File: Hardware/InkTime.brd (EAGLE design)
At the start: 46 x 35 mm, 105 parts, among them IC1 BQ25180YBGR, IC2 DRV2605YZFR, IC3 BMA423, IC9 RT6160AWSC, J1 503480-2400, J2 TC2030-IDC, J4 KH-TYPE-C-16P, Q1 20V/4.2A/52mΩ/1.4W, Q3 SI1308EDL-T1-GE3, U1 NRF52840_QF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

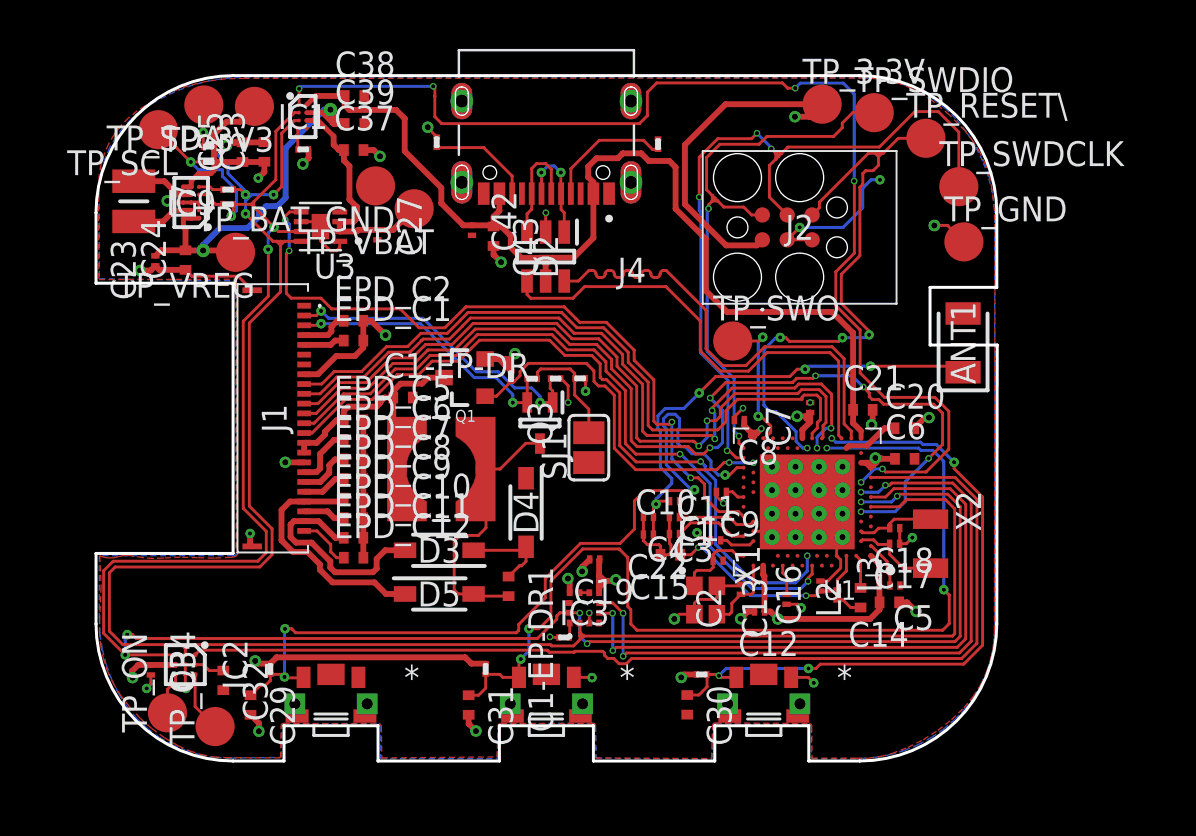
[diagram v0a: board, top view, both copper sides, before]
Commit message: Fixed #1. Added README.md, and updated the schematic and PCB design as stated in the issue.
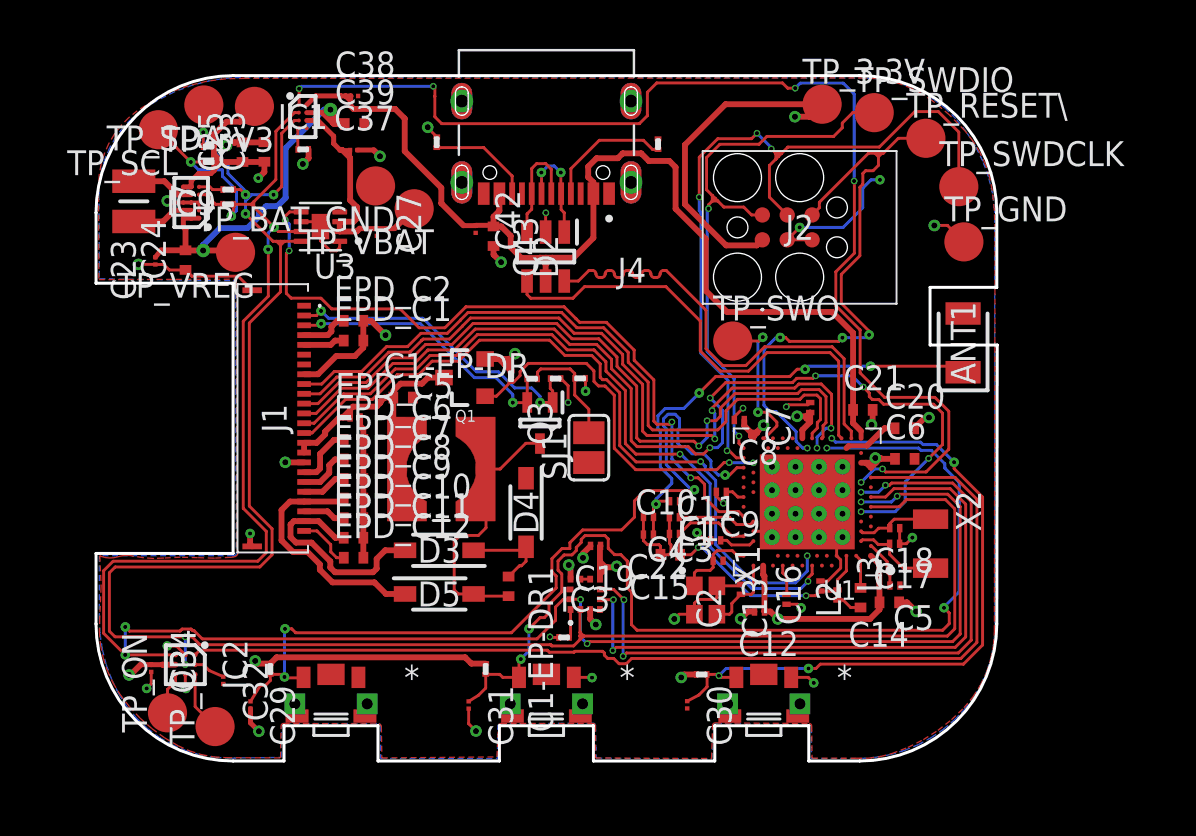
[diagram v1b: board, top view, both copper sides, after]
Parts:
- C23, C27, C34, C42: device InkTime_v5:NORDIC_NRF_3_RESC0201_L -> InkTime_v5:GRM011R60J152KE01L_2_CAPC0201X13N
- C29, C30, C31, C32, C37, C38: device InkTime_v5:NORDIC_NRF_3_RESC0402_L -> InkTime_v5:GRM011R60J152KE01L_2_CAPC0201X13N
- EPD_C5: value 1uF/50V -> 0.1uF/50V; device InkTime_v5:NORDIC_NRF_3_RESC0402_L -> InkTime_v5:NORDIC_NRF_3_RESC0201_L
- moved C19 0.69 mm to (2.51, -6.51)
- moved IC3 0.69 mm to (1.98, -8.99)
- moved C42 0.20 mm to (-3.61, 9.66)
- moved EPD_C5 0.17 mm to (-9.77, 0.04)
- moved C27 0.13 mm to (-8.66, 9.50)
- moved C34 0.09 mm to (-20.2, -12.8)
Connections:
- net GND: now also IC2.B1; no longer IC2.B2
- net SDA: now also IC2.B2; no longer IC2.B1
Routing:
- net GND: track 76.8 -> 80.1 mm, vias 35 -> 36
- net P0.14: track 48.8 -> 50.8 mm
- net SCL: track 110.0 -> 112.0 mm
- net 3V3: track 71.7 -> 73.3 mm
- net SDA: track 104.8 -> 105.7 mm, vias 4 -> 6
- net VBAT: track 12.3 -> 13.1 mm
- net N$4: track 0.74 -> 1.45 mm
- net IMU_INT2: track 35.0 -> 35.7 mm
- net IMU_INT1: track 33.1 -> 33.7 mm
- net P1.02: track 42.6 -> 43.1 mm
